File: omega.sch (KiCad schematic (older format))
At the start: 61 parts, among them SW1 SW_Push, U1 ProMicro

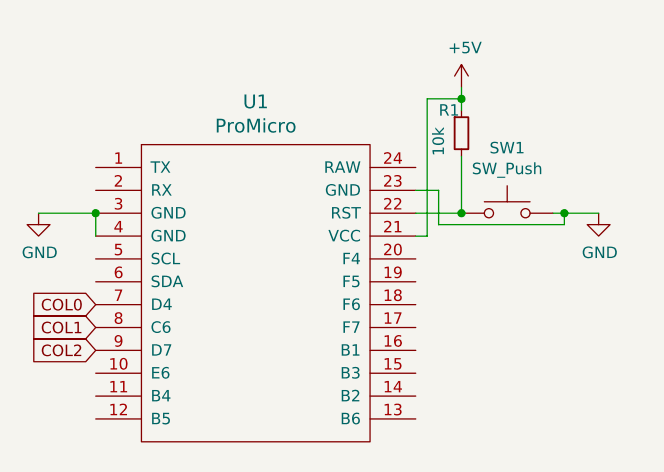
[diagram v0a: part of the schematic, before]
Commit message: flip pro micor and generate assembly files
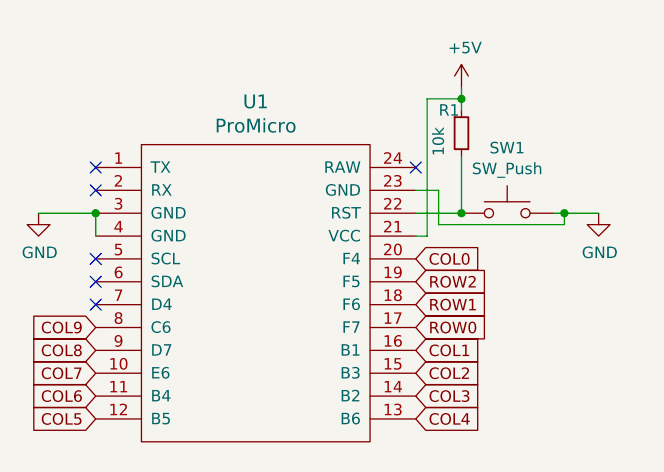
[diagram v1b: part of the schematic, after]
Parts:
- D1, D10, D11, D12, D13, D14, D15, D16, D17, D18, D19, D2, D20, D21, D22, D23, D24, D25, D26, D27, D28, D29, D3, D4, D5, D6, D7, D8, D9: footprint Diode_SMD:D_SOD-123 -> Diode_THT:D_DO-35_SOD27_P3.81mm_Vertical_AnodeUp
- R1: footprint Resistor_SMD:R_0805_2012Metric -> Resistor_THT:R_Axial_DIN0204_L3.6mm_D1.6mm_P5.08mm_Horizontal
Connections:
- net COL0: now also U1.20 (F4); no longer U1.7 (D4)
- net COL1: now also U1.16 (B1); no longer U1.8 (C6)
- net COL2: now also U1.15 (B3); no longer U1.9 (D7)
- net COL3: now also U1.14 (B2)
- net COL4: now also U1.13 (B6)
- net COL5: now also U1.12 (B5)
- net COL6: now also U1.11 (B4)
- net COL7: now also U1.10 (E6)
- net COL8: now also U1.9 (D7)
- net COL9: now also U1.8 (C6)
- net ROW0: now also U1.17 (F7)
- net ROW1: now also U1.18 (F6)
- net ROW2: now also U1.19 (F5)
- no-connect marks 0 -> 6
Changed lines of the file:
@@
 F 0 "D1" V 6146 1582 50  0000 R CNN
 F 1 "D_Small" V 6055 1582 50  0000 R CNN
-F 2 "Diode_SMD:D_SOD-123" V 6100 1650 50  0001 C CNN
+F 2 "Diode_THT:D_DO-35_SOD27_P3.81mm_Vertical_AnodeUp" V 6100 1650 50  0001 C CNN
 F 3 "~" V 6100 1650 50  0001 C CNN
 	1    6100 1650
@@
 F 0 "D11" V 6146 2232 50  0000 R CNN
 F 1 "D_Small" V 6055 2232 50  0000 R CNN
-F 2 "Diode_SMD:D_SOD-123" V 6100 2300 50  0001 C CNN
+F 2 "Diode_THT:D_DO-35_SOD27_P3.81mm_Vertical_AnodeUp" V 6100 2300 50  0001 C CNN
 F 3 "~" V 6100 2300 50  0001 C CNN
 	1    6100 2300
@@
 F 0 "D21" V 6146 2832 50  0000 R CNN
 F 1 "D_Small" V 6055 2832 50  0000 R CNN
-F 2 "Diode_SMD:D_SOD-123" V 6100 2900 50  0001 C CNN
+F 2 "Diode_THT:D_DO-35_SOD27_P3.81mm_Vertical_AnodeUp" V 6100 2900 50  0001 C CNN
 F 3 "~" V 6100 2900 50  0001 C CNN
 	1    6100 2900
@@
 F 0 "D2" V 6596 1582 50  0000 R CNN
 F 1 "D_Small" V 6505 1582 50  0000 R CNN
-F 2 "Diode_SMD:D_SOD-123" V 6550 1650 50  0001 C CNN
+F 2 "Diode_THT:D_DO-35_SOD27_P3.81mm_Vertical_AnodeUp" V 6550 1650 50  0001 C CNN
 F 3 "~" V 6550 1650 50  0001 C CNN
 	1    6550 1650
@@
 F 0 "D12" V 6596 2232 50  0000 R CNN
 F 1 "D_Small" V 6505 2232 50  0000 R CNN
-F 2 "Diode_SMD:D_SOD-123" V 6550 2300 50  0001 C CNN
+F 2 "Diode_THT:D_DO-35_SOD27_P3.81mm_Vertical_AnodeUp" V 6550 2300 50  0001 C CNN
 F 3 "~" V 6550 2300 50  0001 C CNN
 	1    6550 2300
@@
 F 0 "D22" V 6596 2832 50  0000 R CNN
 F 1 "D_Small" V 6505 2832 50  0000 R CNN
-F 2 "Diode_SMD:D_SOD-123" V 6550 2900 50  0001 C CNN
+F 2 "Diode_THT:D_DO-35_SOD27_P3.81mm_Vertical_AnodeUp" V 6550 2900 50  0001 C CNN
 F 3 "~" V 6550 2900 50  0001 C CNN
 	1    6550 2900
@@
 F 0 "D3" V 7046 1582 50  0000 R CNN
 F 1 "D_Small" V 6955 1582 50  0000 R CNN
-F 2 "Diode_SMD:D_SOD-123" V 7000 1650 50  0001 C CNN
+F 2 "Diode_THT:D_DO-35_SOD27_P3.81mm_Vertical_AnodeUp" V 7000 1650 50  0001 C CNN
 F 3 "~" V 7000 1650 50  0001 C CNN
 	1    7000 1650
@@
 F 0 "D13" V 7046 2232 50  0000 R CNN
 F 1 "D_Small" V 6955 2232 50  0000 R CNN
-F 2 "Diode_SMD:D_SOD-123" V 7000 2300 50  0001 C CNN
+F 2 "Diode_THT:D_DO-35_SOD27_P3.81mm_Vertical_AnodeUp" V 7000 2300 50  0001 C CNN
 F 3 "~" V 7000 2300 50  0001 C CNN
 	1    7000 2300
@@
 F 0 "D23" V 7046 2832 50  0000 R CNN
 F 1 "D_Small" V 6955 2832 50  0000 R CNN
-F 2 "Diode_SMD:D_SOD-123" V 7000 2900 50  0001 C CNN
+F 2 "Diode_THT:D_DO-35_SOD27_P3.81mm_Vertical_AnodeUp" V 7000 2900 50  0001 C CNN
 F 3 "~" V 7000 2900 50  0001 C CNN
 	1    7000 2900
@@
 F 0 "D4" V 7496 1582 50  0000 R CNN
 F 1 "D_Small" V 7405 1582 50  0000 R CNN
-F 2 "Diode_SMD:D_SOD-123" V 7450 1650 50  0001 C CNN
+F 2 "Diode_THT:D_DO-35_SOD27_P3.81mm_Vertical_AnodeUp" V 7450 1650 50  0001 C CNN
 F 3 "~" V 7450 1650 50  0001 C CNN
 	1    7450 1650
@@
 F 0 "D14" V 7496 2232 50  0000 R CNN
 F 1 "D_Small" V 7405 2232 50  0000 R CNN
-F 2 "Diode_SMD:D_SOD-123" V 7450 2300 50  0001 C CNN
+F 2 "Diode_THT:D_DO-35_SOD27_P3.81mm_Vertical_AnodeUp" V 7450 2300 50  0001 C CNN
 F 3 "~" V 7450 2300 50  0001 C CNN
 	1    7450 2300
@@
 F 0 "D24" V 7496 2832 50  0000 R CNN
 F 1 "D_Small" V 7405 2832 50  0000 R CNN
-F 2 "Diode_SMD:D_SOD-123" V 7450 2900 50  0001 C CNN
+F 2 "Diode_THT:D_DO-35_SOD27_P3.81mm_Vertical_AnodeUp" V 7450 2900 50  0001 C CNN
 F 3 "~" V 7450 2900 50  0001 C CNN
 	1    7450 2900
@@
 F 0 "D5" V 7946 1582 50  0000 R CNN
 F 1 "D_Small" V 7855 1582 50  0000 R CNN
-F 2 "Diode_SMD:D_SOD-123" V 7900 1650 50  0001 C CNN
+F 2 "Diode_THT:D_DO-35_SOD27_P3.81mm_Vertical_AnodeUp" V 7900 1650 50  0001 C CNN
 F 3 "~" V 7900 1650 50  0001 C CNN
 	1    7900 1650
@@
 F 0 "D15" V 7946 2232 50  0000 R CNN
 F 1 "D_Small" V 7855 2232 50  0000 R CNN
-F 2 "Diode_SMD:D_SOD-123" V 7900 2300 50  0001 C CNN
+F 2 "Diode_THT:D_DO-35_SOD27_P3.81mm_Vertical_AnodeUp" V 7900 2300 50  0001 C CNN
 F 3 "~" V 7900 2300 50  0001 C CNN
 	1    7900 2300
@@
 F 0 "D25" V 7946 2832 50  0000 R CNN
 F 1 "D_Small" V 7855 2832 50  0000 R CNN
-F 2 "Diode_SMD:D_SOD-123" V 7900 2900 50  0001 C CNN
+F 2 "Diode_THT:D_DO-35_SOD27_P3.81mm_Vertical_AnodeUp" V 7900 2900 50  0001 C CNN
 F 3 "~" V 7900 2900 50  0001 C CNN
 	1    7900 2900
@@
 F 0 "D6" V 8396 1582 50  0000 R CNN
 F 1 "D_Small" V 8305 1582 50  0000 R CNN
-F 2 "Diode_SMD:D_SOD-123" V 8350 1650 50  0001 C CNN
+F 2 "Diode_THT:D_DO-35_SOD27_P3.81mm_Vertical_AnodeUp" V 8350 1650 50  0001 C CNN
 F 3 "~" V 8350 1650 50  0001 C CNN
 	1    8350 1650
@@
 F 0 "D16" V 8396 2232 50  0000 R CNN
 F 1 "D_Small" V 8305 2232 50  0000 R CNN
-F 2 "Diode_SMD:D_SOD-123" V 8350 2300 50  0001 C CNN
+F 2 "Diode_THT:D_DO-35_SOD27_P3.81mm_Vertical_AnodeUp" V 8350 2300 50  0001 C CNN
 F 3 "~" V 8350 2300 50  0001 C CNN
 	1    8350 2300
@@
 F 0 "D7" V 8846 1582 50  0000 R CNN
 F 1 "D_Small" V 8755 1582 50  0000 R CNN
-F 2 "Diode_SMD:D_SOD-123" V 8800 1650 50  0001 C CNN
+F 2 "Diode_THT:D_DO-35_SOD27_P3.81mm_Vertical_AnodeUp" V 8800 1650 50  0001 C CNN
 F 3 "~" V 8800 1650 50  0001 C CNN
 	1    8800 1650
@@
 F 0 "D17" V 8846 2232 50  0000 R CNN
 F 1 "D_Small" V 8755 2232 50  0000 R CNN
-F 2 "Diode_SMD:D_SOD-123" V 8800 2300 50  0001 C CNN
+F 2 "Diode_THT:D_DO-35_SOD27_P3.81mm_Vertical_AnodeUp" V 8800 2300 50  0001 C CNN
 F 3 "~" V 8800 2300 50  0001 C CNN
 	1    8800 2300
@@
 F 0 "D26" V 8846 2832 50  0000 R CNN
 F 1 "D_Small" V 8755 2832 50  0000 R CNN
-F 2 "Diode_SMD:D_SOD-123" V 8800 2900 50  0001 C CNN
+F 2 "Diode_THT:D_DO-35_SOD27_P3.81mm_Vertical_AnodeUp" V 8800 2900 50  0001 C CNN
 F 3 "~" V 8800 2900 50  0001 C CNN
 	1    8800 2900
@@
 F 0 "D8" V 9296 1582 50  0000 R CNN
 F 1 "D_Small" V 9205 1582 50  0000 R CNN
-F 2 "Diode_SMD:D_SOD-123" V 9250 1650 50  0001 C CNN
+F 2 "Diode_THT:D_DO-35_SOD27_P3.81mm_Vertical_AnodeUp" V 9250 1650 50  0001 C CNN
 F 3 "~" V 9250 1650 50  0001 C CNN
 	1    9250 1650
@@
 F 0 "D18" V 9296 2232 50  0000 R CNN
 F 1 "D_Small" V 9205 2232 50  0000 R CNN
-F 2 "Diode_SMD:D_SOD-123" V 9250 2300 50  0001 C CNN
+F 2 "Diode_THT:D_DO-35_SOD27_P3.81mm_Vertical_AnodeUp" V 9250 2300 50  0001 C CNN
 F 3 "~" V 9250 2300 50  0001 C CNN
 	1    9250 2300
@@
 F 0 "D27" V 9296 2832 50  0000 R CNN
 F 1 "D_Small" V 9205 2832 50  0000 R CNN
-F 2 "Diode_SMD:D_SOD-123" V 9250 2900 50  0001 C CNN
+F 2 "Diode_THT:D_DO-35_SOD27_P3.81mm_Vertical_AnodeUp" V 9250 2900 50  0001 C CNN
 F 3 "~" V 9250 2900 50  0001 C CNN
 	1    9250 2900
@@
 F 0 "D9" V 9746 1582 50  0000 R CNN
 F 1 "D_Small" V 9655 1582 50  0000 R CNN
-F 2 "Diode_SMD:D_SOD-123" V 9700 1650 50  0001 C CNN
+F 2 "Diode_THT:D_DO-35_SOD27_P3.81mm_Vertical_AnodeUp" V 9700 1650 50  0001 C CNN
 F 3 "~" V 9700 1650 50  0001 C CNN
 	1    9700 1650
@@
 F 0 "D19" V 9746 2232 50  0000 R CNN
 F 1 "D_Small" V 9655 2232 50  0000 R CNN
-F 2 "Diode_SMD:D_SOD-123" V 9700 2300 50  0001 C CNN
+F 2 "Diode_THT:D_DO-35_SOD27_P3.81mm_Vertical_AnodeUp" V 9700 2300 50  0001 C CNN
 F 3 "~" V 9700 2300 50  0001 C CNN
 	1    9700 2300
@@
 F 0 "D28" V 9746 2832 50  0000 R CNN
 F 1 "D_Small" V 9655 2832 50  0000 R CNN
-F 2 "Diode_SMD:D_SOD-123" V 9700 2900 50  0001 C CNN
+F 2 "Diode_THT:D_DO-35_SOD27_P3.81mm_Vertical_AnodeUp" V 9700 2900 50  0001 C CNN
 F 3 "~" V 9700 2900 50  0001 C CNN
 	1    9700 2900
@@
 F 0 "D10" V 10196 1582 50  0000 R CNN
 F 1 "D_Small" V 10105 1582 50  0000 R CNN
-F 2 "Diode_SMD:D_SOD-123" V 10150 1650 50  0001 C CNN
+F 2 "Diode_THT:D_DO-35_SOD27_P3.81mm_Vertical_AnodeUp" V 10150 1650 50  0001 C CNN
 F 3 "~" V 10150 1650 50  0001 C CNN
 	1    10150 1650
@@
 F 0 "D20" V 10196 2232 50  0000 R CNN
 F 1 "D_Small" V 10105 2232 50  0000 R CNN
-F 2 "Diode_SMD:D_SOD-123" V 10150 2300 50  0001 C CNN
+F 2 "Diode_THT:D_DO-35_SOD27_P3.81mm_Vertical_AnodeUp" V 10150 2300 50  0001 C CNN
 F 3 "~" V 10150 2300 50  0001 C CNN
 	1    10150 2300
@@
 F 0 "D29" V 10196 2832 50  0000 R CNN
 F 1 "D_Small" V 10105 2832 50  0000 R CNN
-F 2 "Diode_SMD:D_SOD-123" V 10150 2900 50  0001 C CNN
+F 2 "Diode_THT:D_DO-35_SOD27_P3.81mm_Vertical_AnodeUp" V 10150 2900 50  0001 C CNN
 F 3 "~" V 10150 2900 50  0001 C CNN
 	1    10150 2900
@@
 F 0 "R1" H 3600 1750 50  0000 L CNN
 F 1 "10k" V 3600 1550 50  0000 L CNN
-F 2 "Resistor_SMD:R_0805_2012Metric" H 3700 1650 50  0001 C CNN
+F 2 "Resistor_THT:R_Axial_DIN0204_L3.6mm_D1.6mm_P5.08mm_Horizontal" H 3700 1650 50  0001 C CNN
 F 3 "~" H 3700 1650 50  0001 C CNN
 	1    3700 1650
@@
 Wire Wire Line
 	3700 1500 3700 1550
-Text GLabel 2100 2400 0    50   Input ~ 0
-COL0
-Text GLabel 2100 2500 0    50   Input ~ 0
+Text GLabel 2100 2800 0    50   Input ~ 0
+COL6
+Text GLabel 3500 2600 2    50   Input ~ 0
 COL1
 Text GLabel 2100 2600 0    50   Input ~ 0
+COL8
+Text GLabel 2100 2500 0    50   Input ~ 0
+COL9
+Text GLabel 3500 2700 2    50   Input ~ 0
 COL2
+Text GLabel 3500 2500 2    50   Input ~ 0
+ROW0
+Text GLabel 3500 2200 2    50   Input ~ 0
+COL0
+Text GLabel 3500 2300 2    50   Input ~ 0
+ROW2
+Text GLabel 3500 2400 2    50   Input ~ 0
+ROW1
+Text GLabel 2100 2700 0    50   Input ~ 0
+COL7
+Text GLabel 2100 2900 0    50   Input ~ 0
+COL5
+Text GLabel 3500 2900 2    50   Input ~ 0
+COL4
+Text GLabel 3500 2800 2    50   Input ~ 0
+COL3
+NoConn ~ 2100 2200
+NoConn ~ 2100 2300
+NoConn ~ 2100 2400
+NoConn ~ 2100 1900
+NoConn ~ 2100 1800
+NoConn ~ 3500 1800
 $EndSCHEMATC
